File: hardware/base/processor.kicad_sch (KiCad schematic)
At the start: 10 parts, among them SW1 RESET, SW2 BOOT, SW4 NAV, U6 ESP32-S3-WROOM-1

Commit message: schematic complete unreviewed
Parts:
- removed R40: R_Small, Resistor_SMD:R_0402_1005Metric, symbol Device:R_Small
- removed U6: ESP32-S3-WROOM-1, bt_Espressif:ESP32-S3-WROOM-1U, symbol bt_Espressif:ESP32-S3-WROOM-1
- added D7, D8: LED_Small_Filled, LED_SMD:LED_0603_1608Metric, symbol Device:LED_Small_Filled
- added J4: Debug UART, Connector_PinHeader_2.54mm:PinHeader_1x03_P2.54mm_Vertical, symbol Connector_Generic:Conn_01x03
- added R2, R7: 1k, Resistor_SMD:R_0402_1005Metric, symbol Device:R_Small
- added R8: 100k, Resistor_SMD:R_0402_1005Metric, symbol Device:R_Small
- added U1: PI4IOE5V9554A, Package_SO:TSSOP-16_4.4x5mm_P0.65mm, symbol Interface_Expansion:TCA9554PW
- added U3: ESP32-S3-WROOM-1-PinOrder, bt_Espressif:ESP32-S3-WROOM-1U, symbol bt_Espressif:ESP32-S3-WROOM-1-PinOrder
- D6: footprint LED_SMD:LED_0402_1005Metric -> LED_SMD:LED_0603_1608Metric; Label STAT -> STATUS_ESP
- R1, R6: value R_Small -> 100k
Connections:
- net BMS_INT: now also U1.9 (P4)
- net BOOT_BTN: now also U3.27 (GPIO0/BOOT)
- net DISPLAY_BL: now also U3.38 (GPIO2/TOUCH2/ADC1_CH1)
- net GND: now also D7.1 (K), D8.1 (K), J4.1 (Pin_1), U1.1 (A0), U1.2 (A1), U1.3 (A2), U1.8 (GND), U3.1 (GND), U3.40 (GND), U3.41 (GND)
- net GPS_UART.RX: now also U3.10 (GPIO17/U1TXD/ADC2_CH6)
- net GPS_UART.TX: now also U3.11 (GPIO18/U1RXD/ADC2_CH7/CLK_OUT3)
- net NAV_BTN: now also R8.2, U1.5 (P1)
- net POWER_BUTTON: now also U3.39 (GPIO1/TOUCH1/ADC1_CH0)
- net SDMMC.CLK: now also U3.7 (GPIO7/TOUCH7/ADC1_CH6)
- net SDMMC.CMD: now also U3.6 (GPIO6/TOUCH6/ADC1_CH5)
- net SDMMC.D0: now also U3.8 (GPIO15/U0RTS/ADC2_CH4/XTAL_32K_P)
- net SDMMC.D1: now also U3.9 (GPIO16/U0CTS/ADC2_CH5/XTAL_32K_NH5)
- net SDMMC.D2: now also U3.5 (GPIO5/TOUCH5/ADC1_CH4)
- net SDMMC.D3: now also U3.4 (GPIO4/TOUCH4/ADC1_CH3)
- net SYS_I2C.SCL: now also U1.14 (SCL), U3.23 (GPIO21)
- net SYS_I2C.SDA: now also U1.15 (SDA), U3.24 (GPIO47/SPICLK_P/SUBSPICLK_P_DIFF)
- net USB_ESP.D+: now also U3.14 (GPIO20/U1CTS/ADC2_CH9/CLK_OUT1/USB_D+)
- net USB_ESP.D-: now also U3.13 (GPIO19/U1RTS/ADC2_CH8/CLK_OUT2/USB_D-)
- net STATUS_ESP: now reaches R41.2
- net STATUS_ESP: now also U3.12 (GPIO8/TOUCH8/ADC1_CH7/SUBSPICS1)
- net +3V3 renamed VDD_CORE_3V3
- net VDD_CORE_3V3: now also R8.1, U1.16 (VDD), U3.2 (3V3)
- net RST_BTN renamed ~{RESET}
- net ~{RESET}: now also U3.3 (EN)
- new net: D7.2 (A), R2.1
- new net: D8.2 (A), R7.1
- new net AUX_REG_EN: U1.11 (P6)
- new net DEBUG_RX: J4.2 (Pin_2), U3.37 (U0TXD/GPIO43/CLK_OUT1)
- new net DEBUG_TX: J4.3 (Pin_3), U3.36 (U0RXD/GPIO44/CLK_OUT2)
- new net GPS_FIX: U1.6 (P2)
- new net GPS_FORCE_ON: U1.7 (P3)
- new net IOEXP_INT: U1.13 (~{INT}), U3.25 (GPIO48/SPICLK_N/SUBSPICLK_N_DIFF)
- new net ISENSE_INT: U1.10 (P5)
- new net LCD_MUX0: U3.32 (MTCK/GPIO39/CLK_OUT3/SUBSPICS1)
- new net LCD_MUX1: U3.33 (MTDO/GPIO40/CLK_OUT2)
- new net LCD_MUX2: U3.34 (MTDI/GPIO41/CLK_OUT1)
- new net LCD_MUX3: U3.35 (MTMS/GPIO42)
- new net LCD_RGB.B0: U3.22 (GPIO14/TOUCH14/ADC2_CH3/FSPIWP/FSPIDQS/SUBSPIWP)
- new net LCD_RGB.B1: U3.21 (GPIO13/TOUCH13/ADC2_CH2/FSPIQ/FSPIIO7/SUBSPIQ)
- new net LCD_RGB.G0: U3.20 (GPIO12/TOUCH12/ADC2_CH1/FSPICLK/FSPIIO6/SUBSPICLK)
- new net LCD_RGB.G1: U3.19 (GPIO11/TOUCH11/ADC2_CH0/FSPID/FSPIIO5/SUBSPID)
- new net LCD_RGB.G2: U3.18 (GPIO10/TOUCH10/ADC1_CH9/FSPICS0/FSPIIO4/SUBSPICS0)
- new net LCD_RGB.R0: U3.17 (GPIO9/TOUCH9/ADC1_CH8/FSPIHD/SUBSPIHD)
- new net LCD_RGB.R1: U3.16 (GPIO46)
- new net LCD_RGB.R2: U3.15 (GPIO3/TOUCH3/ADC1_CH2)
- new net LCD_SPI_CS: U3.31 (GPIO38/FSPIWP/SUBSPIWP)
- new net SHUTDOWN: U1.12 (P7)
- new net STATUS_IOEXP0: R2.2, U1.4 (P0)
- new net STATUS_IOEXP1: R7.2
- new net TOUCH_INT: U3.26 (GPIO45)
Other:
- moved on the sheet: C1, D6, R1, R41, R6, SW1, SW2

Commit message: placed components on board - rough
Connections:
- net LCD_RGB.B0: now also U3.21 (GPIO13/TOUCH13/ADC2_CH2/FSPIQ/FSPIIO7/SUBSPIQ); no longer U3.22 (GPIO14/TOUCH14/ADC2_CH3/FSPIWP/FSPIDQS/SUBSPIWP)
- net LCD_RGB.B1: now also U3.22 (GPIO14/TOUCH14/ADC2_CH3/FSPIWP/FSPIDQS/SUBSPIWP); no longer U3.21 (GPIO13/TOUCH13/ADC2_CH2/FSPIQ/FSPIIO7/SUBSPIQ)
- net LCD_RGB.G0: now also U3.18 (GPIO10/TOUCH10/ADC1_CH9/FSPICS0/FSPIIO4/SUBSPICS0); no longer U3.20 (GPIO12/TOUCH12/ADC2_CH1/FSPICLK/FSPIIO6/SUBSPICLK)
- net LCD_RGB.G2: now also U3.20 (GPIO12/TOUCH12/ADC2_CH1/FSPICLK/FSPIIO6/SUBSPICLK); no longer U3.18 (GPIO10/TOUCH10/ADC1_CH9/FSPICS0/FSPIIO4/SUBSPICS0)
- net LCD_RGB.R0: now also U3.15 (GPIO3/TOUCH3/ADC1_CH2); no longer U3.17 (GPIO9/TOUCH9/ADC1_CH8/FSPIHD/SUBSPIHD)
- net LCD_RGB.R2: now also U3.17 (GPIO9/TOUCH9/ADC1_CH8/FSPIHD/SUBSPIHD); no longer U3.15 (GPIO3/TOUCH3/ADC1_CH2)
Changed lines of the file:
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@@
     (effects (font (size 0.8 0.8)) (justify right bottom))
   )
-  (label "LCD_RGB.R0" (at 52.07 87.63 0)
+  (label "LCD_RGB.R0" (at 52.07 82.55 0)
     (effects (font (size 0.8 0.8)) (justify left bottom))
   )
@@
     (effects (font (size 0.8 0.8)) (justify left bottom))
   )
-  (label "LCD_RGB.R2" (at 52.07 82.55 0)
+  (label "LCD_RGB.R2" (at 52.07 87.63 0)
     (effects (font (size 0.8 0.8)) (justify left bottom))
   )
@@
     (effects (font (size 0.8 0.8)) (justify left bottom))
   )
-  (label "LCD_RGB.G2" (at 52.07 90.17 0)
+  (label "LCD_RGB.G2" (at 52.07 95.25 0)
     (effects (font (size 0.8 0.8)) (justify left bottom))
   )
@@
     (effects (font (size 0.8 0.8)) (justify left bottom))
   )
-  (label "LCD_RGB.B1" (at 52.07 97.79 0)
+  (label "LCD_RGB.B1" (at 52.07 100.33 0)
     (effects (font (size 0.8 0.8)) (justify left bottom))
   )
-  (label "LCD_RGB.B0" (at 52.07 100.33 0)
+  (label "LCD_RGB.B0" (at 52.07 97.79 0)
     (effects (font (size 0.8 0.8)) (justify left bottom))
   )
@@
     (effects (font (size 0.8 0.8)) (justify left bottom))
   )
-  (label "LCD_RGB.G0" (at 52.07 95.25 0)
+  (label "LCD_RGB.G0" (at 52.07 90.17 0)
     (effects (font (size 0.8 0.8)) (justify left bottom))
   )

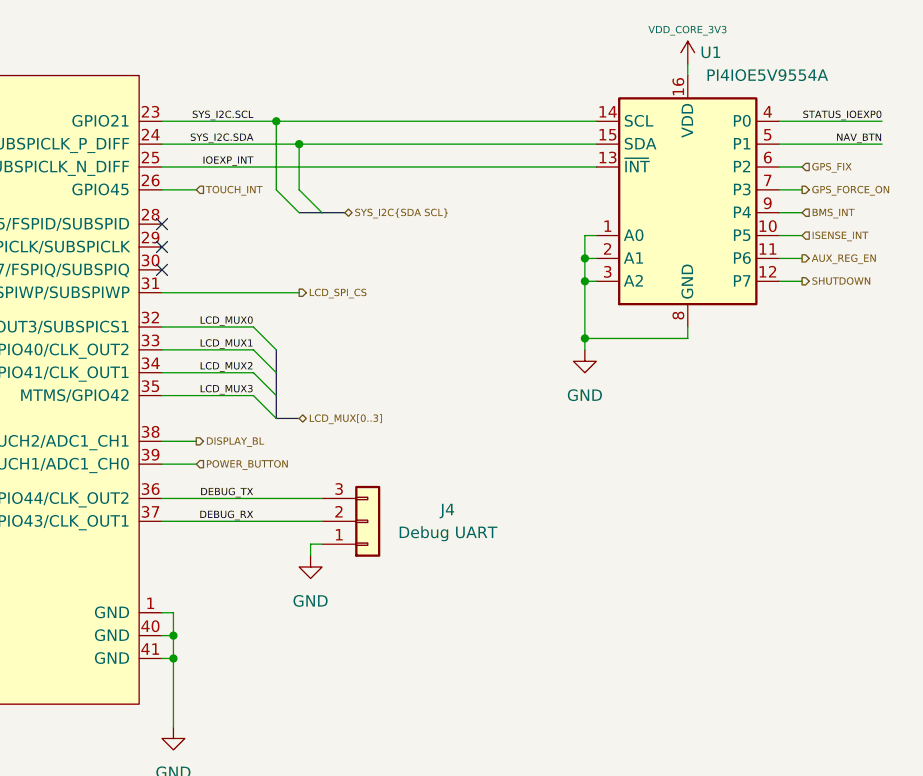
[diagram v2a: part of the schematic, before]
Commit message: Testing condensed layout
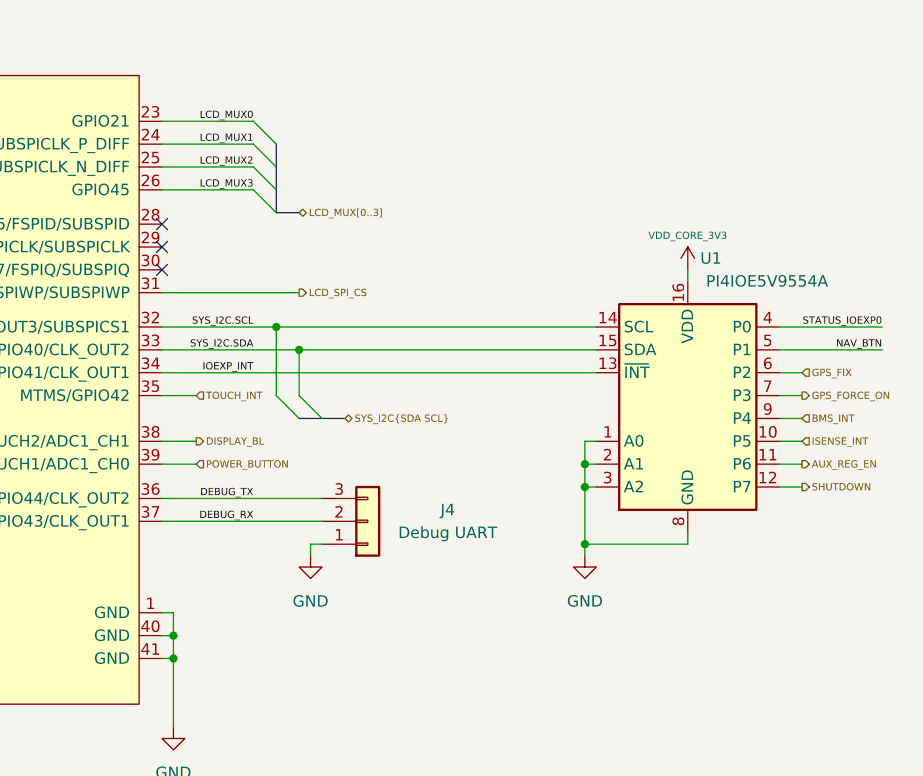
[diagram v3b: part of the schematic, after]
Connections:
- net IOEXP_INT: now also U3.34 (MTDI/GPIO41/CLK_OUT1); no longer U3.25 (GPIO48/SPICLK_N/SUBSPICLK_N_DIFF)
- net LCD_MUX0: now also U3.23 (GPIO21); no longer U3.32 (MTCK/GPIO39/CLK_OUT3/SUBSPICS1)
- net LCD_MUX1: now also U3.24 (GPIO47/SPICLK_P/SUBSPICLK_P_DIFF); no longer U3.33 (MTDO/GPIO40/CLK_OUT2)
- net LCD_MUX2: now also U3.25 (GPIO48/SPICLK_N/SUBSPICLK_N_DIFF); no longer U3.34 (MTDI/GPIO41/CLK_OUT1)
- net LCD_MUX3: now also U3.26 (GPIO45); no longer U3.35 (MTMS/GPIO42)
- net SYS_I2C.SCL: now also U3.32 (MTCK/GPIO39/CLK_OUT3/SUBSPICS1); no longer U3.23 (GPIO21)
- net SYS_I2C.SDA: now also U3.33 (MTDO/GPIO40/CLK_OUT2); no longer U3.24 (GPIO47/SPICLK_P/SUBSPICLK_P_DIFF)
- net TOUCH_INT: now also U3.35 (MTMS/GPIO42); no longer U3.26 (GPIO45)
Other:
- moved on the sheet: U1

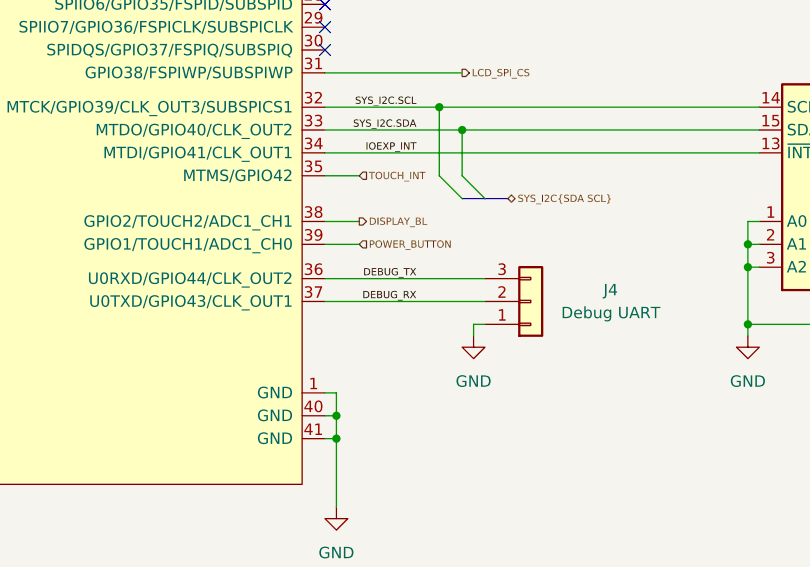
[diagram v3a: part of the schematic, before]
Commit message: split back out condensed board into lcdboard and base
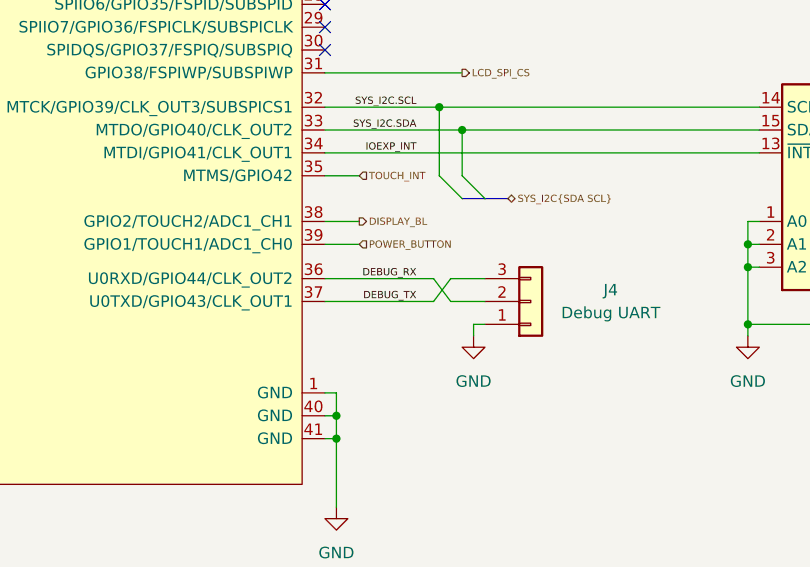
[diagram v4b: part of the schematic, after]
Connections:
- net DEBUG_RX: now also U3.36 (U0RXD/GPIO44/CLK_OUT2); no longer U3.37 (U0TXD/GPIO43/CLK_OUT1)
- net DEBUG_TX: now also U3.37 (U0TXD/GPIO43/CLK_OUT1); no longer U3.36 (U0RXD/GPIO44/CLK_OUT2)
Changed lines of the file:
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@@
+    (stroke (width 0) (type default) (color 0 0 0 0))
+  )
+  (wire (pts (xy 196.85 88.9) (xy 200.66 88.9))
     (stroke (width 0) (type default) (color 0 0 0 0))
   )
@@
     (stroke (width 0) (type default) (color 0 0 0 0))
   )
+  (wire (pts (xy 194.945 91.44) (xy 182.88 91.44))
+    (stroke (width 0) (type default) (color 0 0 0 0))
+  )
   (wire (pts (xy 64.77 77.47) (xy 52.07 77.47))
     (stroke (width 0) (type default) (color 0 0 0 0))
@@
     (stroke (width 0) (type default) (color 0 0 0 0))
   )
+  (wire (pts (xy 196.85 91.44) (xy 200.66 91.44))
+    (stroke (width 0) (type default) (color 0 0 0 0))
+  )
   (wire (pts (xy 118.11 158.75) (xy 128.27 158.75))
     (stroke (width 0) (type default) (color 0 0 0 0))
@@
     (stroke (width 0) (type default) (color 0 0 0 0))
   )
+  (wire (pts (xy 194.945 88.9) (xy 196.85 91.44))
+    (stroke (width 0) (type default) (color 0 0 0 0))
+  )
   (bus (pts (xy 45.72 82.55) (xy 49.53 82.55))
     (stroke (width 0) (type default) (color 0 0 0 0))
@@
     (stroke (width 0) (type default) (color 0 0 0 0))
   )
+  (wire (pts (xy 196.85 88.9) (xy 194.945 91.44))
+    (stroke (width 0) (type default) (color 0 0 0 0))
+  )
   (wire (pts (xy 140.97 158.75) (xy 139.7 158.75))
     (stroke (width 0) (type default) (color 0 0 0 0))
@@
     (stroke (width 0) (type default) (color 0 0 0 0))
   )
-  (wire (pts (xy 182.88 91.44) (xy 200.66 91.44))
-    (stroke (width 0) (type default) (color 0 0 0 0))
-  )
   (wire (pts (xy 39.37 48.26) (xy 39.37 49.53))
     (stroke (width 0) (type default) (color 0 0 0 0))
@@
     (stroke (width 0) (type default) (color 0 0 0 0))
   )
-  (wire (pts (xy 182.88 88.9) (xy 200.66 88.9))
-    (stroke (width 0) (type default) (color 0 0 0 0))
-  )
   (wire (pts (xy 182.88 77.47) (xy 186.69 77.47))
     (stroke (width 0) (type default) (color 0 0 0 0))
@@
     (stroke (width 0) (type default) (color 0 0 0 0))
   )
+  (wire (pts (xy 182.88 88.9) (xy 194.945 88.9))
+    (stroke (width 0) (type default) (color 0 0 0 0))
+  )
   (wire (pts (xy 229.87 93.98) (xy 229.87 87.63))
     (stroke (width 0) (type default) (color 0 0 0 0))
@@
     (effects (font (size 0.8 0.8)) (justify left bottom))
   )
-  (label "DEBUG_TX" (at 193.04 88.9 180)
+  (label "DEBUG_TX" (at 193.04 91.44 180)
     (effects (font (size 0.8 0.8)) (justify right bottom))
   )
@@
     (effects (font (size 0.8 0.8)) (justify right bottom))
   )
-  (label "DEBUG_RX" (at 193.04 91.44 180)
-    (effects (font (size 0.8 0.8)) (justify right bottom))
-  )
+  (label "DEBUG_RX" (at 193.04 88.9 180)
+    (effects (font (size 0.8 0.8)) (justify right bottom))
+  )

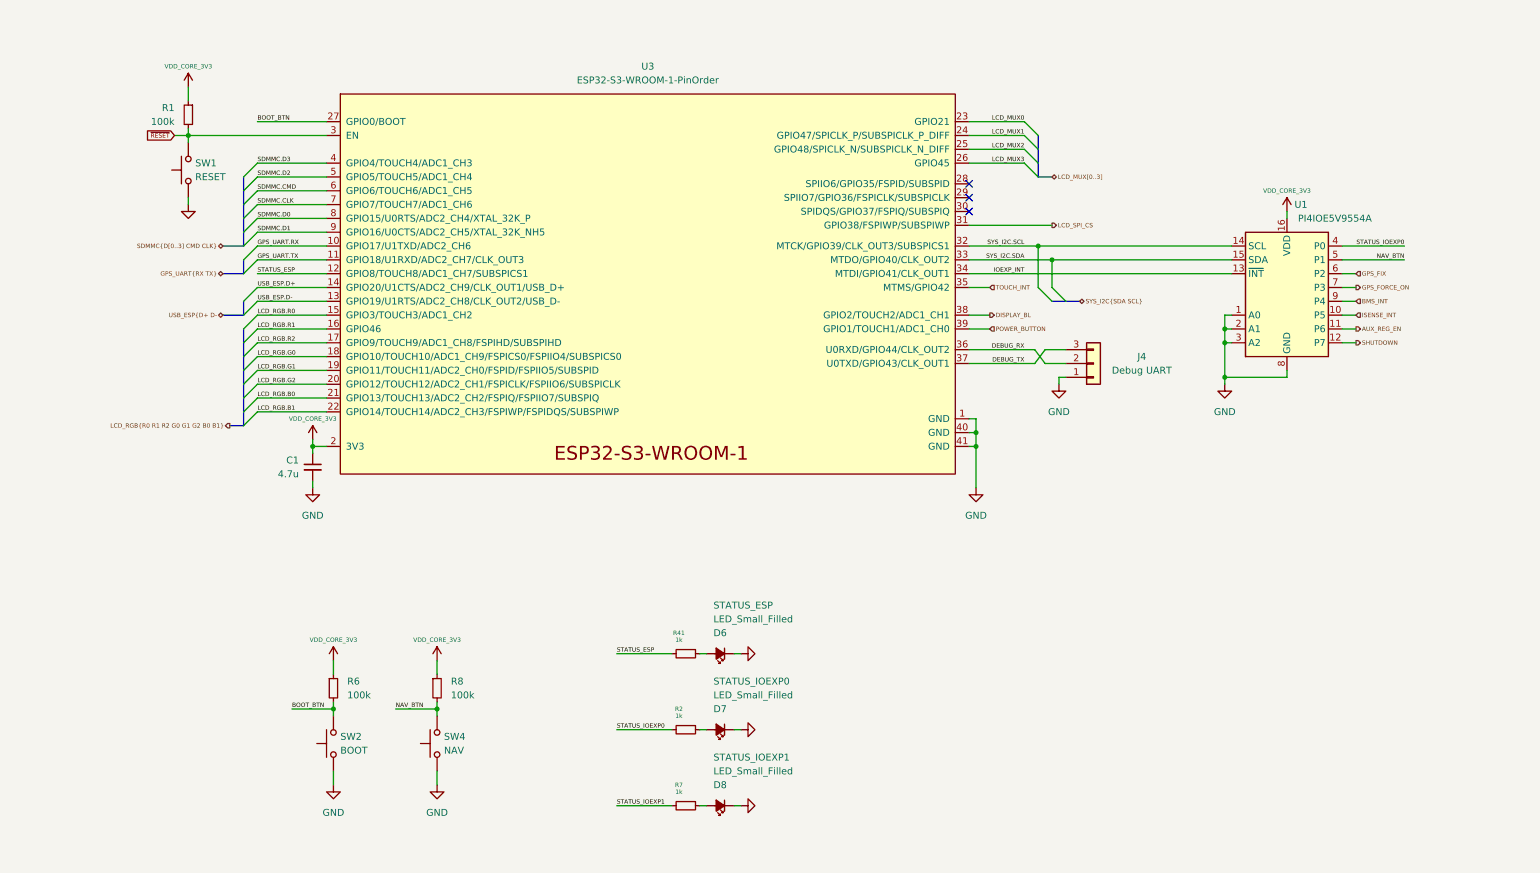
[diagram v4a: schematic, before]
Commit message: screen design freeze, 3d model added to base, routed display connector, sd, usb
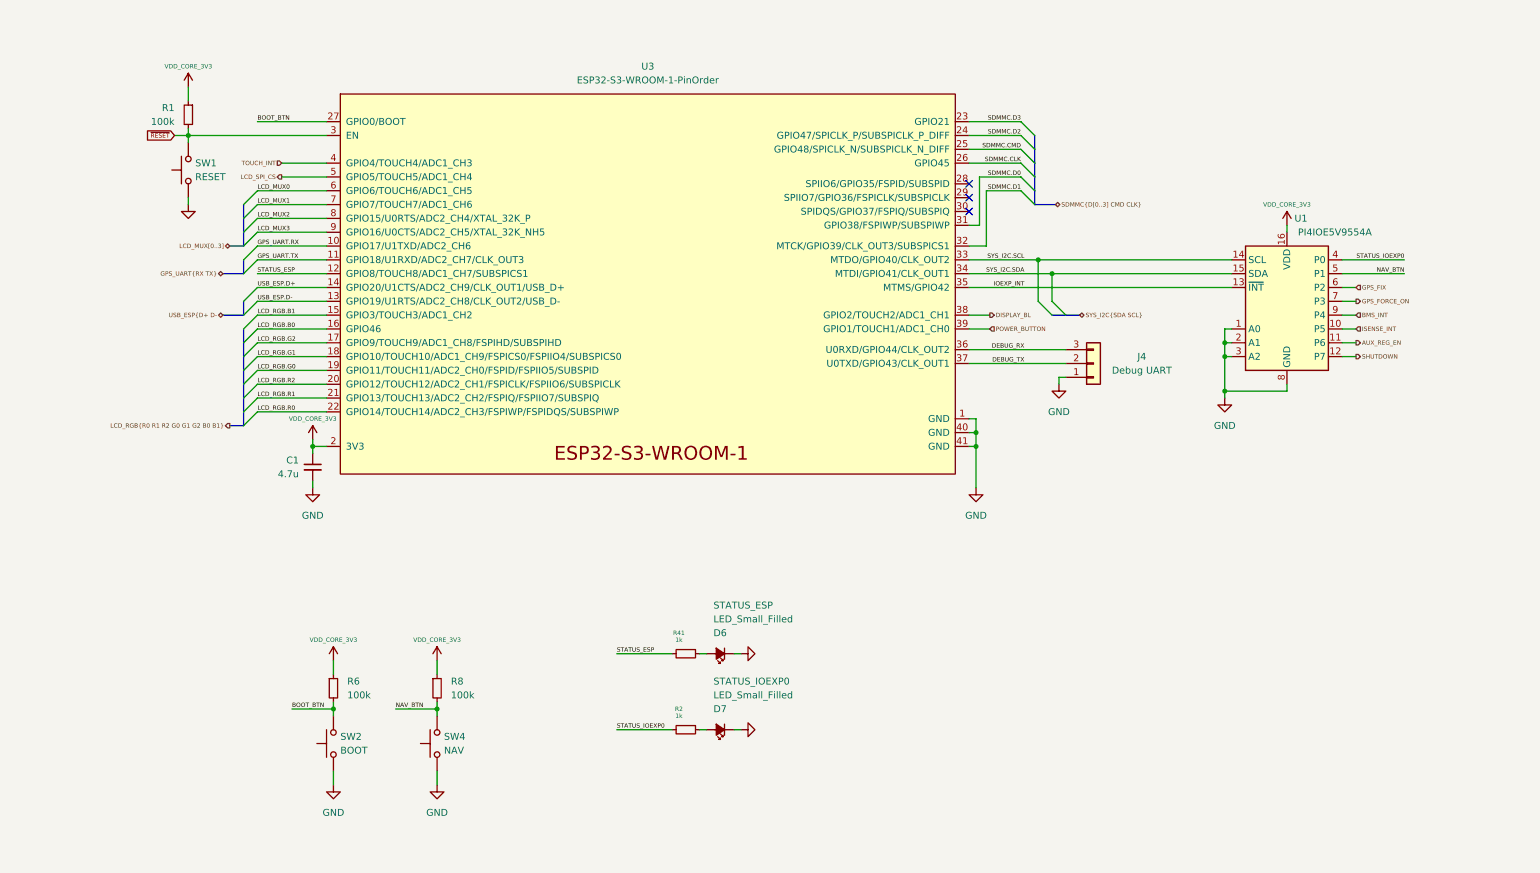
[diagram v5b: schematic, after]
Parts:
- removed D8: LED_Small_Filled, LED_SMD:LED_0603_1608Metric, symbol Device:LED_Small_Filled
- removed R7: 1k, Resistor_SMD:R_0402_1005Metric, symbol Device:R_Small
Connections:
- net DEBUG_RX: now also J4.3 (Pin_3); no longer J4.2 (Pin_2)
- net DEBUG_TX: now also J4.2 (Pin_2); no longer J4.3 (Pin_3)
- net IOEXP_INT: now also U3.35 (MTMS/GPIO42); no longer U3.34 (MTDI/GPIO41/CLK_OUT1)
- net LCD_MUX0: now also U3.6 (GPIO6/TOUCH6/ADC1_CH5); no longer U3.23 (GPIO21)
- net LCD_MUX1: now also U3.7 (GPIO7/TOUCH7/ADC1_CH6); no longer U3.24 (GPIO47/SPICLK_P/SUBSPICLK_P_DIFF)
- net LCD_MUX2: now also U3.8 (GPIO15/U0RTS/ADC2_CH4/XTAL_32K_P); no longer U3.25 (GPIO48/SPICLK_N/SUBSPICLK_N_DIFF)
- net LCD_MUX3: now also U3.9 (GPIO16/U0CTS/ADC2_CH5/XTAL_32K_NH5); no longer U3.26 (GPIO45)
- net LCD_RGB.B0: now also U3.16 (GPIO46); no longer U3.21 (GPIO13/TOUCH13/ADC2_CH2/FSPIQ/FSPIIO7/SUBSPIQ)
- net LCD_RGB.B1: now also U3.15 (GPIO3/TOUCH3/ADC1_CH2); no longer U3.22 (GPIO14/TOUCH14/ADC2_CH3/FSPIWP/FSPIDQS/SUBSPIWP)
- net LCD_RGB.G0: now also U3.19 (GPIO11/TOUCH11/ADC2_CH0/FSPID/FSPIIO5/SUBSPID); no longer U3.18 (GPIO10/TOUCH10/ADC1_CH9/FSPICS0/FSPIIO4/SUBSPICS0)
- net LCD_RGB.G1: now also U3.18 (GPIO10/TOUCH10/ADC1_CH9/FSPICS0/FSPIIO4/SUBSPICS0); no longer U3.19 (GPIO11/TOUCH11/ADC2_CH0/FSPID/FSPIIO5/SUBSPID)
- net LCD_RGB.G2: now also U3.17 (GPIO9/TOUCH9/ADC1_CH8/FSPIHD/SUBSPIHD); no longer U3.20 (GPIO12/TOUCH12/ADC2_CH1/FSPICLK/FSPIIO6/SUBSPICLK)
- net LCD_RGB.R0: now also U3.22 (GPIO14/TOUCH14/ADC2_CH3/FSPIWP/FSPIDQS/SUBSPIWP); no longer U3.15 (GPIO3/TOUCH3/ADC1_CH2)
- net LCD_RGB.R1: now also U3.21 (GPIO13/TOUCH13/ADC2_CH2/FSPIQ/FSPIIO7/SUBSPIQ); no longer U3.16 (GPIO46)
- net LCD_RGB.R2: now also U3.20 (GPIO12/TOUCH12/ADC2_CH1/FSPICLK/FSPIIO6/SUBSPICLK); no longer U3.17 (GPIO9/TOUCH9/ADC1_CH8/FSPIHD/SUBSPIHD)
- net LCD_SPI_CS: now also U3.5 (GPIO5/TOUCH5/ADC1_CH4); no longer U3.31 (GPIO38/FSPIWP/SUBSPIWP)
- net SDMMC.CLK: now also U3.26 (GPIO45); no longer U3.7 (GPIO7/TOUCH7/ADC1_CH6)
- net SDMMC.CMD: now also U3.25 (GPIO48/SPICLK_N/SUBSPICLK_N_DIFF); no longer U3.6 (GPIO6/TOUCH6/ADC1_CH5)
- net SDMMC.D0: now also U3.31 (GPIO38/FSPIWP/SUBSPIWP); no longer U3.8 (GPIO15/U0RTS/ADC2_CH4/XTAL_32K_P)
- net SDMMC.D1: now also U3.32 (MTCK/GPIO39/CLK_OUT3/SUBSPICS1); no longer U3.9 (GPIO16/U0CTS/ADC2_CH5/XTAL_32K_NH5)
- net SDMMC.D2: now also U3.24 (GPIO47/SPICLK_P/SUBSPICLK_P_DIFF); no longer U3.5 (GPIO5/TOUCH5/ADC1_CH4)
- net SDMMC.D3: now also U3.23 (GPIO21); no longer U3.4 (GPIO4/TOUCH4/ADC1_CH3)
- net SYS_I2C.SCL: now also U3.33 (MTDO/GPIO40/CLK_OUT2); no longer U3.32 (MTCK/GPIO39/CLK_OUT3/SUBSPICS1)
- net SYS_I2C.SDA: now also U3.34 (MTDI/GPIO41/CLK_OUT1); no longer U3.33 (MTDO/GPIO40/CLK_OUT2)
- net TOUCH_INT: now also U3.4 (GPIO4/TOUCH4/ADC1_CH3); no longer U3.35 (MTMS/GPIO42)
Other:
- moved on the sheet: U1
